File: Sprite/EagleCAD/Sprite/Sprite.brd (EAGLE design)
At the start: 35 x 35 mm, 23 parts, among them Q1 26MHz, U1 CC430F5137, U2 HMC5883LSMD, U3 ITG-3200

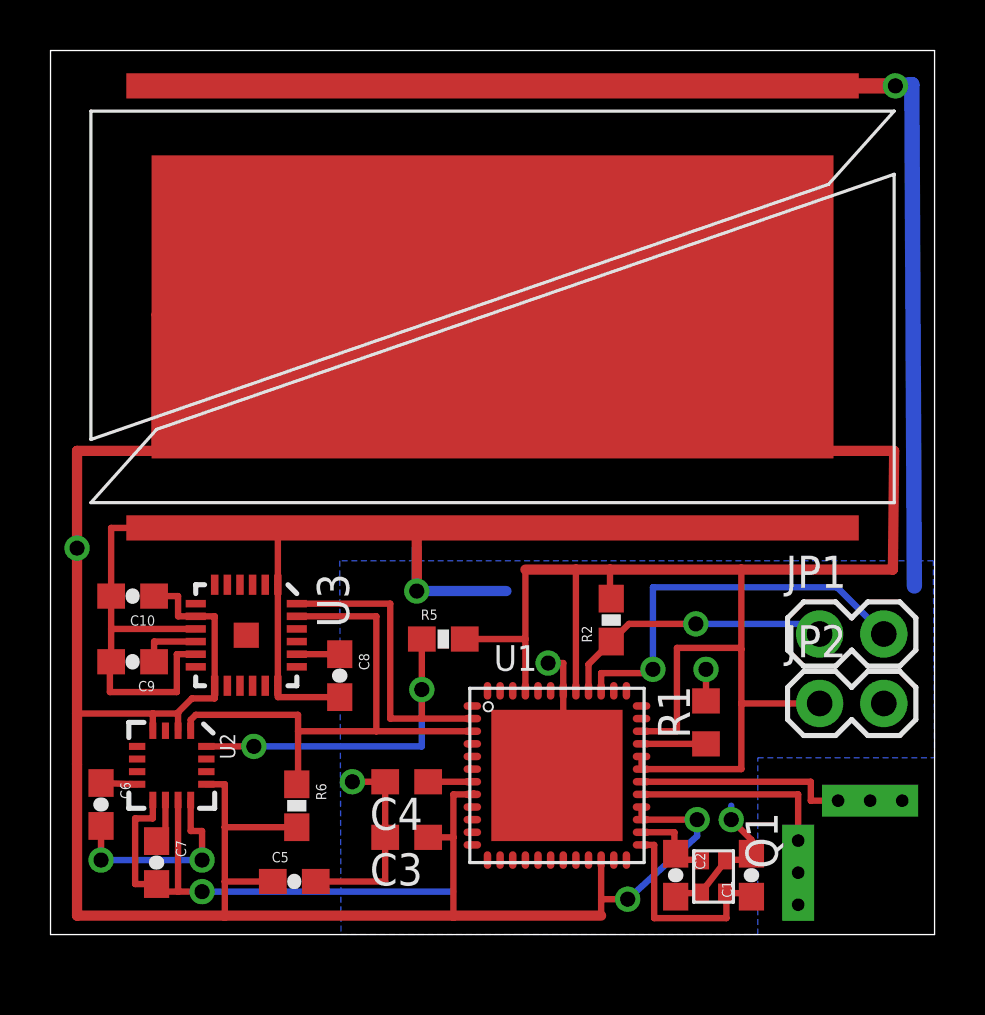
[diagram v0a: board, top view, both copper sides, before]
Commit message: Sprite AVCC_RF Decoupling
Added decoupling caps and inductor to AVCC_RF to decouple from DVCC
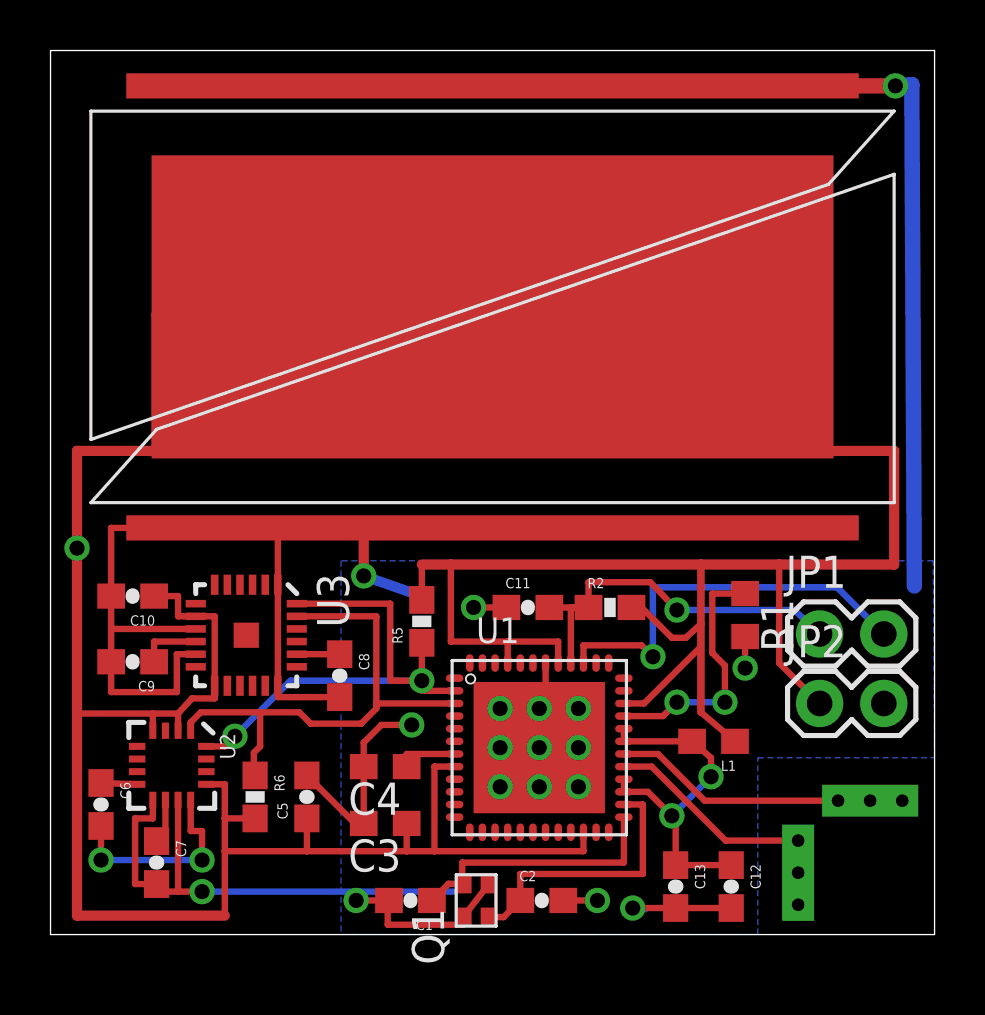
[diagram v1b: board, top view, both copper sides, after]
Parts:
- added C11: 2.2 nF, SparkFun:0603-CAP
- added C12: 100 Nf, SparkFun:0603-CAP
- added C13: 10 Nf, SparkFun:0603-CAP
- added L1: 12 nH, SparkFun:0603
- moved C1 13.5 mm to (14.2, 1.35), turned to 180 degrees
- moved Q1 9.45 mm to (16.9, 1.35), turned to 90 degrees
- moved C2 5.39 mm to (19.4, 1.35), turned to 0 degrees
- moved R1 4.52 mm to (27.5, 12.7), turned to 270 degrees
- moved C5 3.39 mm to (10.2, 5.45), turned to 90 degrees
- moved R6 1.69 mm to (8.10, 5.45)
- moved U1 1.30 mm to (19.4, 7.40)
- moved R5 1.10 mm to (14.7, 12.4), turned to 90 degrees
- moved C4 1.04 mm to (13.2, 6.65)
- moved C3 1.01 mm to (13.2, 4.40)
- moved R2 0.50 mm to (22.1, 12.9), turned to 0 degrees
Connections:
- new net VCCRF: C12.1, C13.1, L1.2, U1.27, U1.28, U1.31, U1.32
- net GND: now also C11.1, C12.2, C13.2
- net RST: now also C11.2
- net VCC: now also L1.1; no longer U1.27, U1.28, U1.31, U1.32
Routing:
- net VCC: track 160.0 -> 145.8 mm, vias 3 -> 1
- net VCCRF: track 0.00 -> 14.2 mm, vias 0 -> 2
- net N$3: track 2.55 -> 10.0 mm, vias 0 -> 2
- net N$1: track 3.74 -> 10.9 mm
- net SDA: track 25.4 -> 20.8 mm
- net RST: track 11.0 -> 15.5 mm
- net N$2: track 8.30 -> 10.6 mm
- net SCL: track 22.2 -> 20.8 mm
- net RFN: track 11.1 -> 11.8 mm
- net N$4: track 1.75 -> 2.40 mm
- net GND: track 131.1 -> 130.9 mm, vias 7 -> 18

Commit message: Updated Gerbers + small tweaks
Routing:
- net VCC: vias 1 -> 0
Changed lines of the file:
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@@
 <wire x1="17.5" y1="24.85" x2="4.2" y2="24.55" width="0.4064" layer="1"/>
 <wire x1="4.2" y1="24.55" x2="4.2" y2="19.15" width="0.4064" layer="1"/>
-<wire x1="4.2" y1="19.15" x2="1.05" y2="19.15" width="0.4064" layer="1"/>
-<wire x1="1.05" y1="19.15" x2="1.05" y2="15.3" width="0.4064" layer="1"/>
-<via x="1.05" y="15.3" extent="1-16" drill="0.6"/>
 <wire x1="33.4" y1="14.65" x2="33.4" y2="19.15" width="0.4064" layer="1"/>
 <wire x1="33.4" y1="19.15" x2="30.7" y2="19.15" width="0.4064" layer="1"/>
@@
 <wire x1="25.75" y1="14.65" x2="15.85" y2="14.65" width="0.4064" layer="1"/>
 <wire x1="15.85" y1="14.65" x2="14.7" y2="14.65" width="0.4064" layer="1"/>
-<wire x1="1.05" y1="15.3" x2="1.05" y2="8.75" width="0.4064" layer="1"/>
 <wire x1="1.05" y1="8.75" x2="1.05" y2="6.75" width="0.4064" layer="1"/>
 <wire x1="1.05" y1="6.75" x2="1.05" y2="0.75" width="0.4064" layer="1"/>
@@
 <wire x1="25.75" y1="12.3" x2="25.75" y2="8.8" width="0.3048" layer="1"/>
 <wire x1="25.75" y1="8.8" x2="27.1" y2="7.65" width="0.254" layer="1"/>
+<wire x1="4.2" y1="19.15" x2="1.05" y2="19.15" width="0.4064" layer="1"/>
+<wire x1="1.05" y1="19.15" x2="1.05" y2="8.75" width="0.4064" layer="1"/>
 <wire x1="25.15" y1="11.75" x2="25.75" y2="11.4" width="0" layer="19" extent="1-1"/>
 <wire x1="16" y1="6.65" x2="18.1" y2="10.75" width="0" layer="19" extent="1-1"/>
@@
 <contactref element="U$2" pad="IN3"/>
 <contactref element="U$2" pad="IN2"/>
-<wire x1="29.6" y1="2.45" x2="29.6" y2="3.72" width="0.254" layer="1"/>
+<wire x1="29.6" y1="2.45" x2="29.6" y2="3.7" width="0.254" layer="1"/>
+<wire x1="29.6" y1="3.7" x2="29.6" y2="3.72" width="0.254" layer="1"/>
 <wire x1="29.6" y1="1.18" x2="29.6" y2="2.45" width="0.254" layer="1"/>
-<wire x1="29.6" y1="3.72" x2="26.73" y2="3.72" width="0.254" layer="1"/>
-<wire x1="26.73" y1="3.72" x2="23.8" y2="6.65" width="0.254" layer="1"/>
 <wire x1="23.8" y1="6.65" x2="22.7" y2="6.65" width="0.254" layer="1"/>
+<wire x1="23.8" y1="6.65" x2="25.75" y2="4.7" width="0.254" layer="1"/>
+<wire x1="25.75" y1="4.7" x2="28.6" y2="4.7" width="0.254" layer="1"/>
+<wire x1="28.6" y1="4.7" x2="29.6" y2="3.7" width="0.254" layer="1"/>
 </signal>
 <signal name="RST">

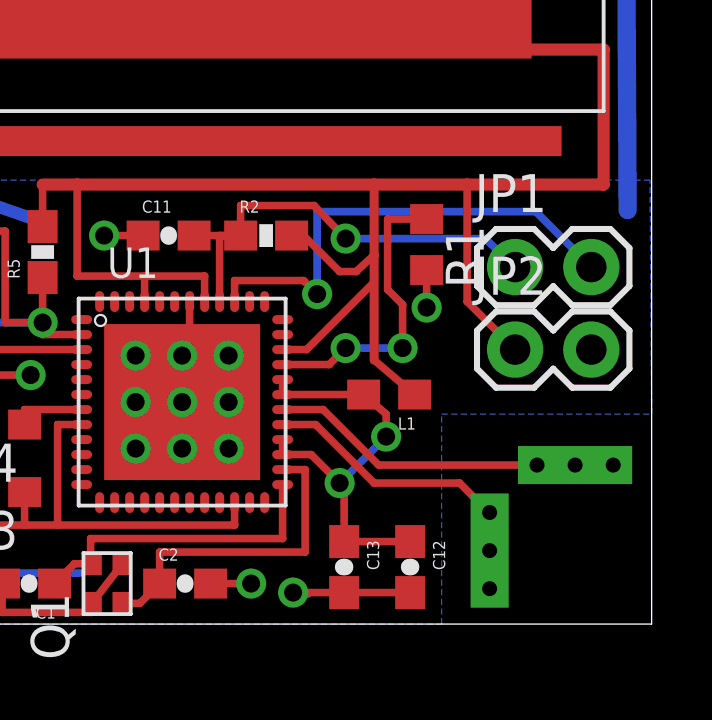
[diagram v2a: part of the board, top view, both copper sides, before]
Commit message: Changed antenna feed line traces to 50 ohm microstrips
Calculated assuming 31 mil board thickness
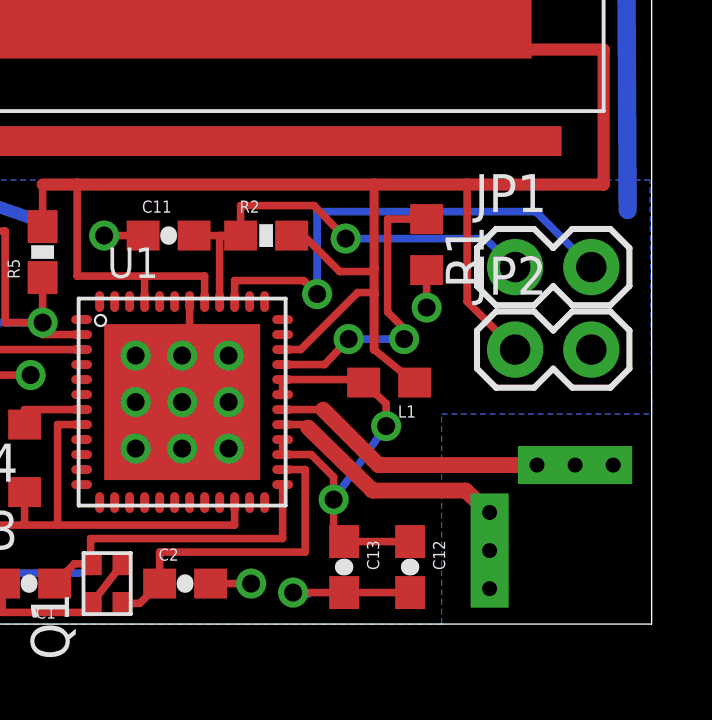
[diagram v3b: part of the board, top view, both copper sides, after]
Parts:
- moved L1 0.40 mm to (26.2, 8.05)
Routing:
- net VCCRF: track 14.2 -> 15.9 mm
- net VCC: track 145.8 -> 145.2 mm
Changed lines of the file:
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@@
 <element name="R2" library="SparkFun" package="0603-RES" value="47K" x="22.15" y="12.95"/>
 <element name="C11" library="SparkFun" package="0603-CAP" value="2.2 nF" x="18.9" y="12.95"/>
-<element name="L1" library="SparkFun" package="0603" value="12 nH" x="26.25" y="7.65" rot="R180"/>
+<element name="L1" library="SparkFun" package="0603" value="12 nH" x="26.25" y="8.05" rot="R180"/>
 <element name="C12" library="SparkFun" package="0603-CAP" value="100 Nf" x="26.95" y="1.9" rot="R270"/>
 <element name="C13" library="SparkFun" package="0603-CAP" value="10 Nf" x="24.75" y="1.9" rot="R270"/>
@@
 <wire x1="30.45" y1="9.15" x2="28.85" y2="10.75" width="0.254" layer="1"/>
 <wire x1="28.85" y1="10.75" x2="28.85" y2="14.65" width="0.254" layer="1"/>
-<wire x1="22.7" y1="9.15" x2="23.5" y2="9.15" width="0.254" layer="1"/>
 <wire x1="23.4" y1="12.95" x2="24.6" y2="11.75" width="0.254" layer="1"/>
-<wire x1="24.6" y1="11.75" x2="25.15" y2="11.75" width="0.254" layer="1"/>
-<wire x1="25.15" y1="11.75" x2="25.75" y2="12.3" width="0.254" layer="1"/>
-<wire x1="23.5" y1="9.15" x2="25.75" y2="11.4" width="0.254" layer="1"/>
 <contactref element="L1" pad="1"/>
-<wire x1="25.75" y1="14.65" x2="25.75" y2="12.3" width="0.3048" layer="1"/>
-<wire x1="25.75" y1="12.3" x2="25.75" y2="8.8" width="0.3048" layer="1"/>
-<wire x1="25.75" y1="8.8" x2="27.1" y2="7.65" width="0.254" layer="1"/>
+<wire x1="25.75" y1="14.65" x2="25.75" y2="11.85" width="0.3048" layer="1"/>
+<wire x1="25.75" y1="11.85" x2="25.75" y2="11" width="0.3048" layer="1"/>
+<wire x1="25.75" y1="11" x2="25.75" y2="9.15" width="0.3048" layer="1"/>
+<wire x1="25.75" y1="9.15" x2="27.1" y2="8.05" width="0.254" layer="1"/>
 <wire x1="4.2" y1="19.15" x2="1.05" y2="19.15" width="0.4064" layer="1"/>
 <wire x1="1.05" y1="19.15" x2="1.05" y2="8.75" width="0.4064" layer="1"/>
-<wire x1="25.15" y1="11.75" x2="25.75" y2="11.4" width="0" layer="19" extent="1-1"/>
+<wire x1="22.7" y1="9.15" x2="23.3" y2="9.15" width="0.254" layer="1"/>
+<wire x1="23.3" y1="9.15" x2="25.2" y2="11.05" width="0.254" layer="1"/>
+<wire x1="25.2" y1="11.05" x2="25.7" y2="11.05" width="0.254" layer="1"/>
+<wire x1="25.7" y1="11.05" x2="25.75" y2="11" width="0.254" layer="1"/>
+<wire x1="24.6" y1="11.75" x2="25.65" y2="11.75" width="0.254" layer="1"/>
+<wire x1="25.65" y1="11.75" x2="25.75" y2="11.85" width="0.254" layer="1"/>
 <wire x1="16" y1="6.65" x2="18.1" y2="10.75" width="0" layer="19" extent="1-1"/>
 </signal>
@@
 <contactref element="R1" pad="1"/>
 <wire x1="27.5" y1="13.5" x2="26.2" y2="13.5" width="0.254" layer="1"/>
-<wire x1="26.2" y1="13.5" x2="26.2" y2="11.15" width="0.254" layer="1"/>
-<wire x1="24.25" y1="8.65" x2="22.7" y2="8.65" width="0.254" layer="1"/>
-<wire x1="24.25" y1="8.65" x2="24.8" y2="9.2" width="0.254" layer="1"/>
-<via x="24.8" y="9.2" extent="1-16" drill="0.6"/>
-<wire x1="24.8" y1="9.2" x2="26.7" y2="9.2" width="0.254" layer="16"/>
-<via x="26.7" y="9.2" extent="1-16" drill="0.6"/>
-<wire x1="26.7" y1="9.2" x2="26.7" y2="10.65" width="0.254" layer="1"/>
-<wire x1="26.7" y1="10.65" x2="26.2" y2="11.15" width="0.254" layer="1"/>
+<wire x1="26.2" y1="13.5" x2="26.2" y2="10.4" width="0.254" layer="1"/>
+<wire x1="24.1" y1="8.65" x2="22.7" y2="8.65" width="0.254" layer="1"/>
+<wire x1="24.1" y1="8.65" x2="24.9" y2="9.5" width="0.254" layer="1"/>
+<via x="24.9" y="9.5" extent="1-16" drill="0.6"/>
+<wire x1="24.9" y1="9.5" x2="26.75" y2="9.5" width="0.254" layer="16"/>
+<via x="26.75" y="9.5" extent="1-16" drill="0.6"/>
+<wire x1="26.75" y1="9.5" x2="26.75" y2="9.85" width="0.254" layer="1"/>
+<wire x1="26.75" y1="9.85" x2="26.2" y2="10.4" width="0.254" layer="1"/>
 </signal>
 <signal name="N$4">
@@
 <contactref element="U$1" pad="IN3"/>
 <contactref element="U$1" pad="IN2"/>
-<wire x1="32.45" y1="5.3" x2="33.72" y2="5.3" width="0.254" layer="1"/>
-<wire x1="31.18" y1="5.3" x2="32.45" y2="5.3" width="0.254" layer="1"/>
-<wire x1="25.9" y1="5.3" x2="31.18" y2="5.3" width="0.254" layer="1"/>
+<wire x1="32.45" y1="5.3" x2="33.72" y2="5.3" width="0.53" layer="1"/>
+<wire x1="31.18" y1="5.3" x2="32.45" y2="5.3" width="0.53" layer="1"/>
+<wire x1="25.9" y1="5.3" x2="31.18" y2="5.3" width="0.53" layer="1"/>
 <wire x1="22.7" y1="7.15" x2="24.05" y2="7.15" width="0.254" layer="1"/>
-<wire x1="24.05" y1="7.15" x2="25.9" y2="5.3" width="0.254" layer="1"/>
+<wire x1="24.05" y1="7.15" x2="25.9" y2="5.3" width="0.53" layer="1"/>
 </signal>
 <signal name="RFP">
@@
 <contactref element="U$2" pad="IN3"/>
 <contactref element="U$2" pad="IN2"/>
-<wire x1="29.6" y1="2.45" x2="29.6" y2="3.7" width="0.254" layer="1"/>
+<wire x1="29.6" y1="2.45" x2="29.6" y2="3.7" width="0.53" layer="1"/>
 <wire x1="29.6" y1="3.7" x2="29.6" y2="3.72" width="0.254" layer="1"/>
-<wire x1="29.6" y1="1.18" x2="29.6" y2="2.45" width="0.254" layer="1"/>
-<wire x1="23.8" y1="6.65" x2="22.7" y2="6.65" width="0.254" layer="1"/>
-<wire x1="23.8" y1="6.65" x2="25.75" y2="4.7" width="0.254" layer="1"/>
-<wire x1="25.75" y1="4.7" x2="28.6" y2="4.7" width="0.254" layer="1"/>
-<wire x1="28.6" y1="4.7" x2="29.6" y2="3.7" width="0.254" layer="1"/>
+<wire x1="29.6" y1="1.18" x2="29.6" y2="2.45" width="0.53" layer="1"/>
+<wire x1="23.55" y1="6.55" x2="25.7" y2="4.45" width="0.53" layer="1"/>
+<wire x1="25.7" y1="4.45" x2="28.8" y2="4.45" width="0.53" layer="1"/>
+<wire x1="28.8" y1="4.45" x2="29.6" y2="3.7" width="0.53" layer="1"/>
+<wire x1="22.7" y1="6.65" x2="23.45" y2="6.65" width="0.254" layer="1"/>
+<wire x1="23.45" y1="6.65" x2="23.55" y2="6.55" width="0.254" layer="1"/>
 </signal>
 <signal name="RST">
@@
 <contactref element="U1" pad="32"/>
 <contactref element="U1" pad="31"/>
-<wire x1="22.7" y1="8.15" x2="22.7" y2="7.7" width="0.254" layer="1"/>
 <contactref element="L1" pad="2"/>
 <contactref element="U1" pad="27"/>
 <contactref element="U1" pad="28"/>
-<wire x1="22.7" y1="7.7" x2="22.7" y2="7.65" width="0.254" layer="1"/>
-<wire x1="25.4" y1="7.65" x2="22.75" y2="7.65" width="0.254" layer="1"/>
-<wire x1="22.75" y1="7.65" x2="22.7" y2="7.7" width="0.254" layer="1"/>
-<wire x1="22.7" y1="5.65" x2="23.65" y2="5.65" width="0.254" layer="1"/>
-<wire x1="23.65" y1="5.65" x2="24.6" y2="4.7" width="0.254" layer="1"/>
-<via x="24.6" y="4.7" extent="1-16" drill="0.6"/>
-<wire x1="24.6" y1="4.7" x2="26.15" y2="6.25" width="0.254" layer="16"/>
-<via x="26.15" y="6.25" extent="1-16" drill="0.6"/>
-<wire x1="26.15" y1="6.25" x2="26.15" y2="7" width="0.254" layer="1"/>
-<wire x1="26.15" y1="7" x2="25.4" y2="7.65" width="0.254" layer="1"/>
+<wire x1="22.7" y1="8.15" x2="22.7" y2="7.65" width="0.254" layer="1"/>
+<wire x1="22.75" y1="7.65" x2="22.7" y2="8.15" width="0.254" layer="1"/>
+<via x="24.4" y="4.15" extent="1-16" drill="0.6"/>
+<wire x1="24.4" y1="4.15" x2="26.15" y2="6.6" width="0.254" layer="16"/>
+<via x="26.15" y="6.6" extent="1-16" drill="0.6"/>
+<wire x1="26.15" y1="6.6" x2="26.15" y2="7.35" width="0.254" layer="1"/>
+<wire x1="26.15" y1="7.35" x2="25.4" y2="8.05" width="0.254" layer="1"/>
 <wire x1="22.7" y1="6.15" x2="22.7" y2="5.65" width="0.254" layer="1"/>
 <contactref element="C12" pad="1"/>
 <contactref element="C13" pad="1"/>
 <wire x1="26.95" y1="2.75" x2="24.75" y2="2.75" width="0.254" layer="1"/>
-<wire x1="24.75" y1="2.75" x2="24.75" y2="4.55" width="0.254" layer="1"/>
-<wire x1="24.75" y1="4.55" x2="24.6" y2="4.7" width="0.254" layer="1"/>
+<wire x1="24.75" y1="2.75" x2="24.4" y2="2.75" width="0.254" layer="1"/>
+<wire x1="24.4" y1="2.75" x2="24.4" y2="4.15" width="0.254" layer="1"/>
+<wire x1="22.7" y1="8.15" x2="25.45" y2="8.15" width="0.254" layer="1"/>
+<wire x1="25.45" y1="8.15" x2="25.4" y2="8.05" width="0.254" layer="1"/>
+<wire x1="22.7" y1="5.65" x2="23.65" y2="5.65" width="0.254" layer="1"/>
+<wire x1="23.65" y1="5.65" x2="24.4" y2="4.9" width="0.254" layer="1"/>
+<wire x1="24.4" y1="4.9" x2="24.4" y2="4.15" width="0.254" layer="1"/>
 </signal>
 </signals>
